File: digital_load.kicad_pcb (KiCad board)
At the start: 2 copper layers, 50 x 45 mm, 24 parts, among them J1 Conn_01x02, J2 Conn_01x02, J3 Conn_01x04, J4 Conn_01x04, J5 USB_C_Receptacle_USB2.0, Q20 BSB280N15NZ3, Q21 Q_NMOS_DGS, Q22 Q_NMOS_DGS, Q23 Q_NMOS_DGS, U10 PIC18F24K42, U20 LM358, U21 Adafruit_PiOLED

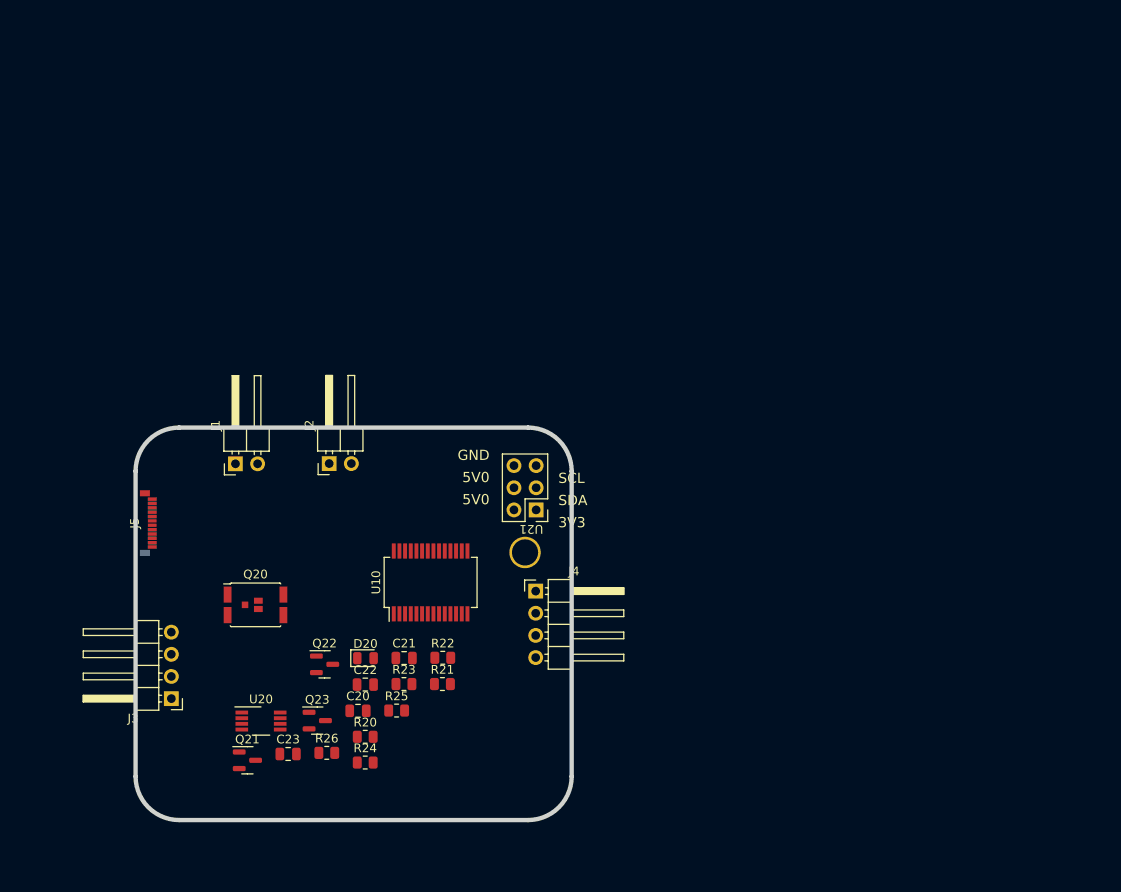
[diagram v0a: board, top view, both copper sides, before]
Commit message: Add uart usb controller
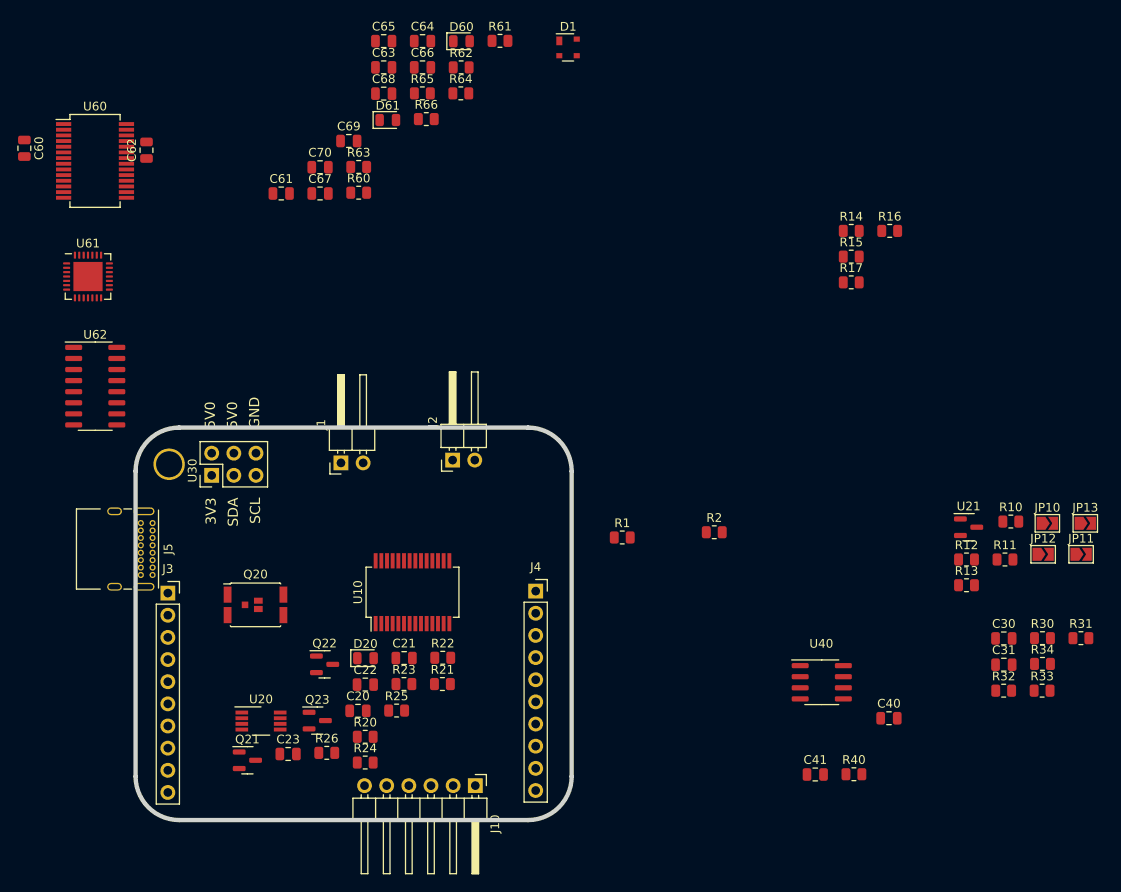
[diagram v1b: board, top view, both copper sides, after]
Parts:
- added C30: 10n, Capacitor_SMD:C_0805_2012Metric, F.Cu at (199.6, 109.2)
- added C31: 10n, Capacitor_SMD:C_0805_2012Metric, F.Cu at (199.6, 112.2)
- added C40: 1u, Capacitor_SMD:C_0805_2012Metric, F.Cu at (186.4, 118.3)
- added C41: 1u, Capacitor_SMD:C_0805_2012Metric, F.Cu at (177.9, 124.8)
- added C60: 4.7u, Capacitor_SMD:C_0805_2012Metric, F.Cu at (87.2, 53.0)
- added C61: 100n, Capacitor_SMD:C_0805_2012Metric, F.Cu at (116.7, 58.2)
- added C62: 100n, Capacitor_SMD:C_0805_2012Metric, F.Cu at (101.2, 53.2)
- added C63: 100n, Capacitor_SMD:C_0805_2012Metric, F.Cu at (128.4, 43.7)
- added C64: 100n, Capacitor_SMD:C_0805_2012Metric, F.Cu at (132.9, 40.7)
- added C65: 100n, Capacitor_SMD:C_0805_2012Metric, F.Cu at (128.4, 40.7)
- added C66: 4.7u, Capacitor_SMD:C_0805_2012Metric, F.Cu at (132.9, 43.7)
- added C67: 4.7u, Capacitor_SMD:C_0805_2012Metric, F.Cu at (121.2, 58.2)
- added C68: 10u, Capacitor_SMD:C_0805_2012Metric, F.Cu at (128.4, 46.7)
- added C69: 100n, Capacitor_SMD:C_0805_2012Metric, F.Cu at (124.5, 52.1)
- added C70: 100n, Capacitor_SMD:C_0805_2012Metric, F.Cu at (121.2, 55.1)
- added D1: SP0503BAHT, Package_TO_SOT_SMD:SOT-143, F.Cu at (149.6, 41.4)
- added D60: LED, LED_SMD:LED_0805_2012Metric, F.Cu at (137.4, 40.7)
- added D61: LED, LED_SMD:LED_0805_2012Metric, F.Cu at (128.9, 49.7)
- added J10: Conn_PIC_ICSP_ICD, Connector_PinHeader_2.54mm:PinHeader_1x06_P2.54mm_Horizontal, F.Cu at (138.9, 126.0)
- added JP10: SolderJumper_2_Open, Jumper:SolderJumper-2_P1.3mm_Open_TrianglePad1.0x1.5mm, F.Cu at (204.5, 96.0)
- added JP11: SolderJumper_2_Open, Jumper:SolderJumper-2_P1.3mm_Open_TrianglePad1.0x1.5mm, F.Cu at (208.4, 99.5)
- added JP12: SolderJumper_2_Open, Jumper:SolderJumper-2_P1.3mm_Open_TrianglePad1.0x1.5mm, F.Cu at (204.1, 99.5)
- added JP13: SolderJumper_2_Open, Jumper:SolderJumper-2_P1.3mm_Open_TrianglePad1.0x1.5mm, F.Cu at (208.9, 96.0)
- added R1: 5.1k, Resistor_SMD:R_0805_2012Metric, F.Cu at (155.8, 97.6)
- added R10: 10k, Resistor_SMD:R_0805_2012Metric, F.Cu at (200.3, 95.8)
- added R11: 10k, Resistor_SMD:R_0805_2012Metric, F.Cu at (199.7, 100.1)
- added R12: 10k, Resistor_SMD:R_0805_2012Metric, F.Cu at (195.3, 100.1)
- added R13: 10k, Resistor_SMD:R_0805_2012Metric, F.Cu at (195.3, 103.1)
- added R14: 10k, Resistor_SMD:R_0805_2012Metric, F.Cu at (182.1, 62.5)
- added R15: 10k, Resistor_SMD:R_0805_2012Metric, F.Cu at (182.1, 65.4)
- added R16: 10k, Resistor_SMD:R_0805_2012Metric, F.Cu at (186.5, 62.5)
- added R17: 4.7k, Resistor_SMD:R_0805_2012Metric, F.Cu at (182.1, 68.3)
- added R2: 5.1k, Resistor_SMD:R_0805_2012Metric, F.Cu at (166.3, 97.0)
- added R30: 10k, Resistor_SMD:R_0805_2012Metric, F.Cu at (204.0, 109.1)
- added R31: 10k, Resistor_SMD:R_0805_2012Metric, F.Cu at (208.4, 109.1)
- added R32: 10k, Resistor_SMD:R_0805_2012Metric, F.Cu at (199.5, 115.2)
- added R33: 10k, Resistor_SMD:R_0805_2012Metric, F.Cu at (203.9, 115.2)
- added R34: 10k, Resistor_SMD:R_0805_2012Metric, F.Cu at (204.0, 112.1)
- added R40: 10k, Resistor_SMD:R_0805_2012Metric, F.Cu at (182.4, 124.7)
- added R60: 4.7k, Resistor_SMD:R_0805_2012Metric, F.Cu at (125.6, 58.1)
- added R61: 10k, Resistor_SMD:R_0805_2012Metric, F.Cu at (141.8, 40.7)
- added R62: 22.1k, Resistor_SMD:R_0805_2012Metric, F.Cu at (137.3, 43.7)
- added R63: 47.5k, Resistor_SMD:R_0805_2012Metric, F.Cu at (125.6, 55.1)
- added R64: 1k, Resistor_SMD:R_0805_2012Metric, F.Cu at (137.3, 46.7)
- added R65: 10k, Resistor_SMD:R_0805_2012Metric, F.Cu at (132.9, 46.7)
- added R66: 10k, Resistor_SMD:R_0805_2012Metric, F.Cu at (133.3, 49.6)
- added U21: LM4040DBZ-2.0, Package_TO_SOT_SMD:SOT-23, F.Cu at (195.5, 96.4)
- added U40: LP2951-3.3_SOIC, Package_SO:SOIC-8_3.9x4.9mm_P1.27mm, F.Cu at (178.7, 114.2)
- added U60: FT232RL, Package_SO:SSOP-28_5.3x10.2mm_P0.65mm, F.Cu at (95.3, 54.4)
- added U61: CP2102N-Axx-xQFN28, Package_DFN_QFN:QFN-28-1EP_5x5mm_P0.5mm_EP3.35x3.35mm, F.Cu at (94.5, 67.7)
- added U62: CH340C, Package_SO:SOIC-16_3.9x9.9mm_P1.27mm, F.Cu at (95.4, 80.2)
- J3, J4: footprint Connector_PinHeader_2.54mm:PinHeader_1x04_P2.54mm_Horizontal -> Connector_PinSocket_2.54mm:PinSocket_1x10_P2.54mm_Vertical
- J5: footprint Connector_USB:USB_C_Plug_Molex_105444 -> Connector_USB:USB_C_Receptacle_GCT_USB4085
- moved U30 37.4 mm to (108.7, 90.5), turned to 90 degrees
- moved J2 14.2 mm to (136.3, 88.7)
- moved J3 12.1 mm to (103.7, 104.0), turned to 0 degrees
- moved J1 12.1 mm to (123.5, 89.0)
- moved U10 2.36 mm to (131.8, 103.9)
- renumbered U21 to U30
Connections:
- J3 pad 1: /Connectors/load_in -> /Connectors/I2C.SCL
- J3 pad 2: /Connectors/TXL -> /Connectors/I2C.SDA
- J3 pad 3: /Connectors/RXL -> +5V
- J3 pad 4: /Connectors/leader_present -> +5V
- J4 pad 2: /Connectors/TXR -> /Connectors/load_in
- J4 pad 3: /Connectors/RXR -> /Connectors/load_in
- J4 pad 4: /Connectors/follower_present -> /Connectors/load_in
- J5 pad A1: Net-(J5-PadA1) -> GND
- J5 pad A12: Net-(J5-PadA1) -> GND
- J5 pad A4: Net-(J5-PadA4) -> +5V
- J5 pad A5: unconnected-(J5-PadA5) -> Net-(J5-PadA5)
- J5 pad A6: unconnected-(J5-PadA6) -> /Connectors/USB2.0.D+
- J5 pad A7: unconnected-(J5-PadA7) -> /Connectors/USB2.0.D-
- J5 pad A9: Net-(J5-PadA4) -> +5V
- J5 pad B1: Net-(J5-PadA1) -> GND
- J5 pad B12: Net-(J5-PadA1) -> GND
- J5 pad B4: Net-(J5-PadA4) -> +5V
- J5 pad B5: unconnected-(J5-PadB5) -> Net-(J5-PadB5)
- J5 pad B9: Net-(J5-PadA4) -> +5V
- J5 pad S1: unconnected-(J5-PadS1) -> GND
- Q21 pad 2: /load_control/range_1ma -> /load_control/range.1ma
- Q22 pad 2: /load_control/range_100ma -> /load_control/range.100ma
- Q23 pad 2: /load_control/range_10a -> /load_control/range.10a
- U10 pad 1: unconnected-(U10-Pad1) -> /microcontroller/~{MCLR}/VPP
- U10 pad 10: unconnected-(U10-Pad10) -> /Display_Encoder/select
- U10 pad 14: /microcontroller/I2C.SCL -> /Connectors/I2C.SCL
- U10 pad 15: /microcontroller/I2C.SDA -> /Connectors/I2C.SDA
- U10 pad 17: /microcontroller/UARTL.TX -> unconnected-(U10-Pad17)
- U10 pad 18: /microcontroller/UARTL.RX -> unconnected-(U10-Pad18)
- U10 pad 21: /microcontroller/pwm_ctrl -> /load_control/pwm_ctrl
- U10 pad 22: /microcontroller/range_1ma -> /load_control/range.1ma
- U10 pad 23: /microcontroller/range_100ma -> /load_control/range.100ma
- U10 pad 24: /microcontroller/range_10a -> /load_control/range.10a
- U10 pad 25: unconnected-(U10-Pad25) -> /load_control/current_measure
- U10 pad 27: /microcontroller/UARTR.TX -> /microcontroller/ICSPCLK
- U10 pad 28: /microcontroller/UARTR.RX -> /microcontroller/ICSPDAT
- U10 pad 5: unconnected-(U10-Pad5) -> /microcontroller/2.048V
- U10 pad 6: unconnected-(U10-Pad6) -> /microcontroller/3V3_sense
- U10 pad 7: unconnected-(U10-Pad7) -> /microcontroller/5V_sense
- U30 pad 3: /Display/I2C.SDA -> /Connectors/I2C.SDA
- U30 pad 5: /Display/I2C.SCL -> /Connectors/I2C.SCL

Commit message: Fix lots of small things
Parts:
- added C10: 100n, Capacitor_SMD:C_0805_2012Metric, F.Cu at (108.7, 50.2)
- added SW30: PEC11R, Rotary_Encoder:RotaryEncoder_Alps_EC12E-Switch_Vertical_H20mm, F.Cu at (164.8, 81.5)
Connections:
- C60 pad 1: /Connectors/USB2.0.VBUS -> +5V
- C62 pad 1: /Connectors/USB2.0.VBUS -> +5V
- C63 pad 1: /Connectors/USB2.0.VBUS -> +5V
- C64 pad 1: /Connectors/USB2.0.VBUS -> +5V
- C65 pad 1: /Connectors/USB2.0.VBUS -> +5V
- C66 pad 1: /Connectors/USB2.0.VBUS -> +5V
- C67 pad 1: /Connectors/USB2.0.VBUS -> +5V
- C68 pad 1: /Connectors/USB2.0.VBUS -> +5V
- C69 pad 1: /Connectors/USB2.0.VBUS -> +5V
- D60 pad 2: /Connectors/USB2.0.VBUS -> +5V
- D61 pad 2: /Connectors/USB2.0.VBUS -> +5V
- Q20 pad 1: /load_control/load_in -> /Connectors/load_in
- R60 pad 2: /Connectors/USB2.0.VBUS -> +5V
- R62 pad 2: /Connectors/USB2.0.VBUS -> +5V
- R64 pad 2: /Connectors/USB2.0.VBUS -> +5V
- U10 pad 10: /Display_Encoder/select -> unconnected-(U10-Pad10)
- U10 pad 13: unconnected-(U10-Pad13) -> /microcontroller/UART.RTS
- U10 pad 16: unconnected-(U10-Pad16) -> /microcontroller/UART.TX
- U10 pad 17: unconnected-(U10-Pad17) -> /microcontroller/UART.CTS
- U10 pad 18: unconnected-(U10-Pad18) -> /microcontroller/UART.RX
- U10 pad 21: /load_control/pwm_ctrl -> /Display_Encoder/ENC.B
- U10 pad 26: unconnected-(U10-Pad26) -> /load_control/pwm_ctrl
- U10 pad 3: unconnected-(U10-Pad3) -> /Display_Encoder/select
- U10 pad 4: unconnected-(U10-Pad4) -> /Display_Encoder/ENC.A
- U60 pad 20: /Connectors/USB2.0.VBUS -> +5V
- U60 pad 4: /Connectors/USB2.0.VBUS -> +5V
- U61 pad 6: /Connectors/USB2.0.VBUS -> +5V
- U61 pad 7: /Connectors/USB2.0.VBUS -> +5V
- U62 pad 16: /Connectors/USB2.0.VBUS -> +5V

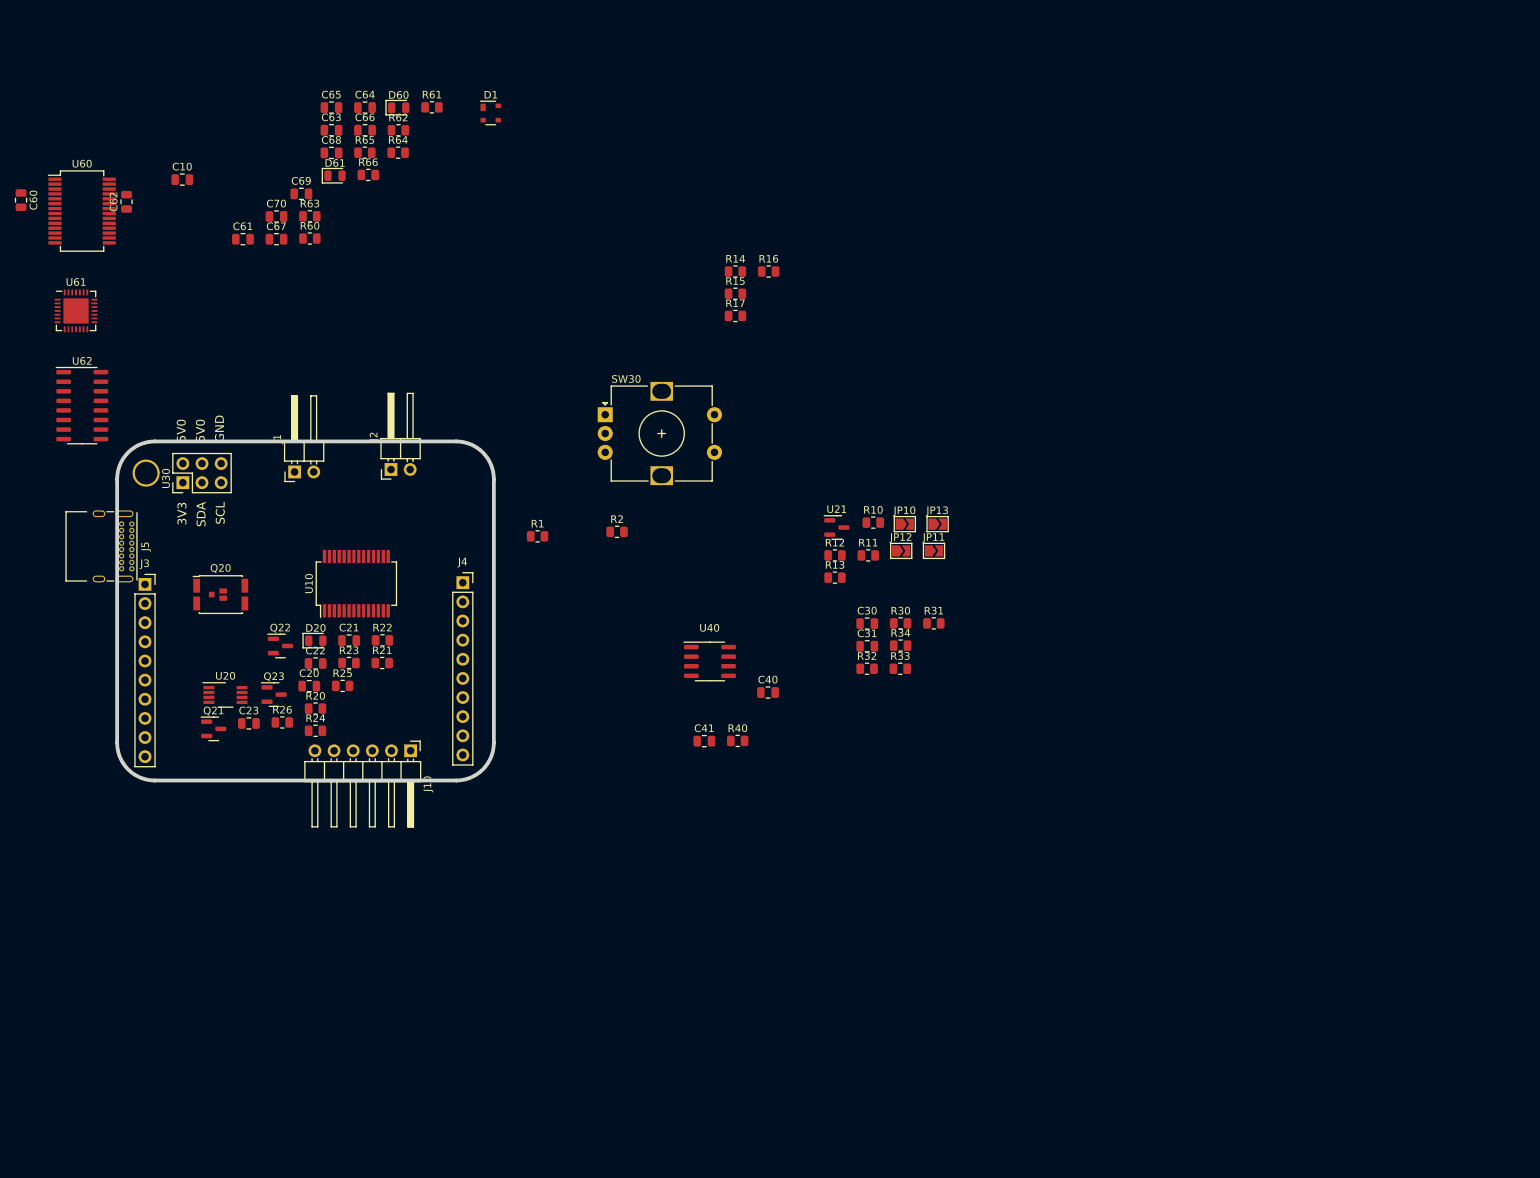
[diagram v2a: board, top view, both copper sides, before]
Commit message: Arrange components of subcircuits
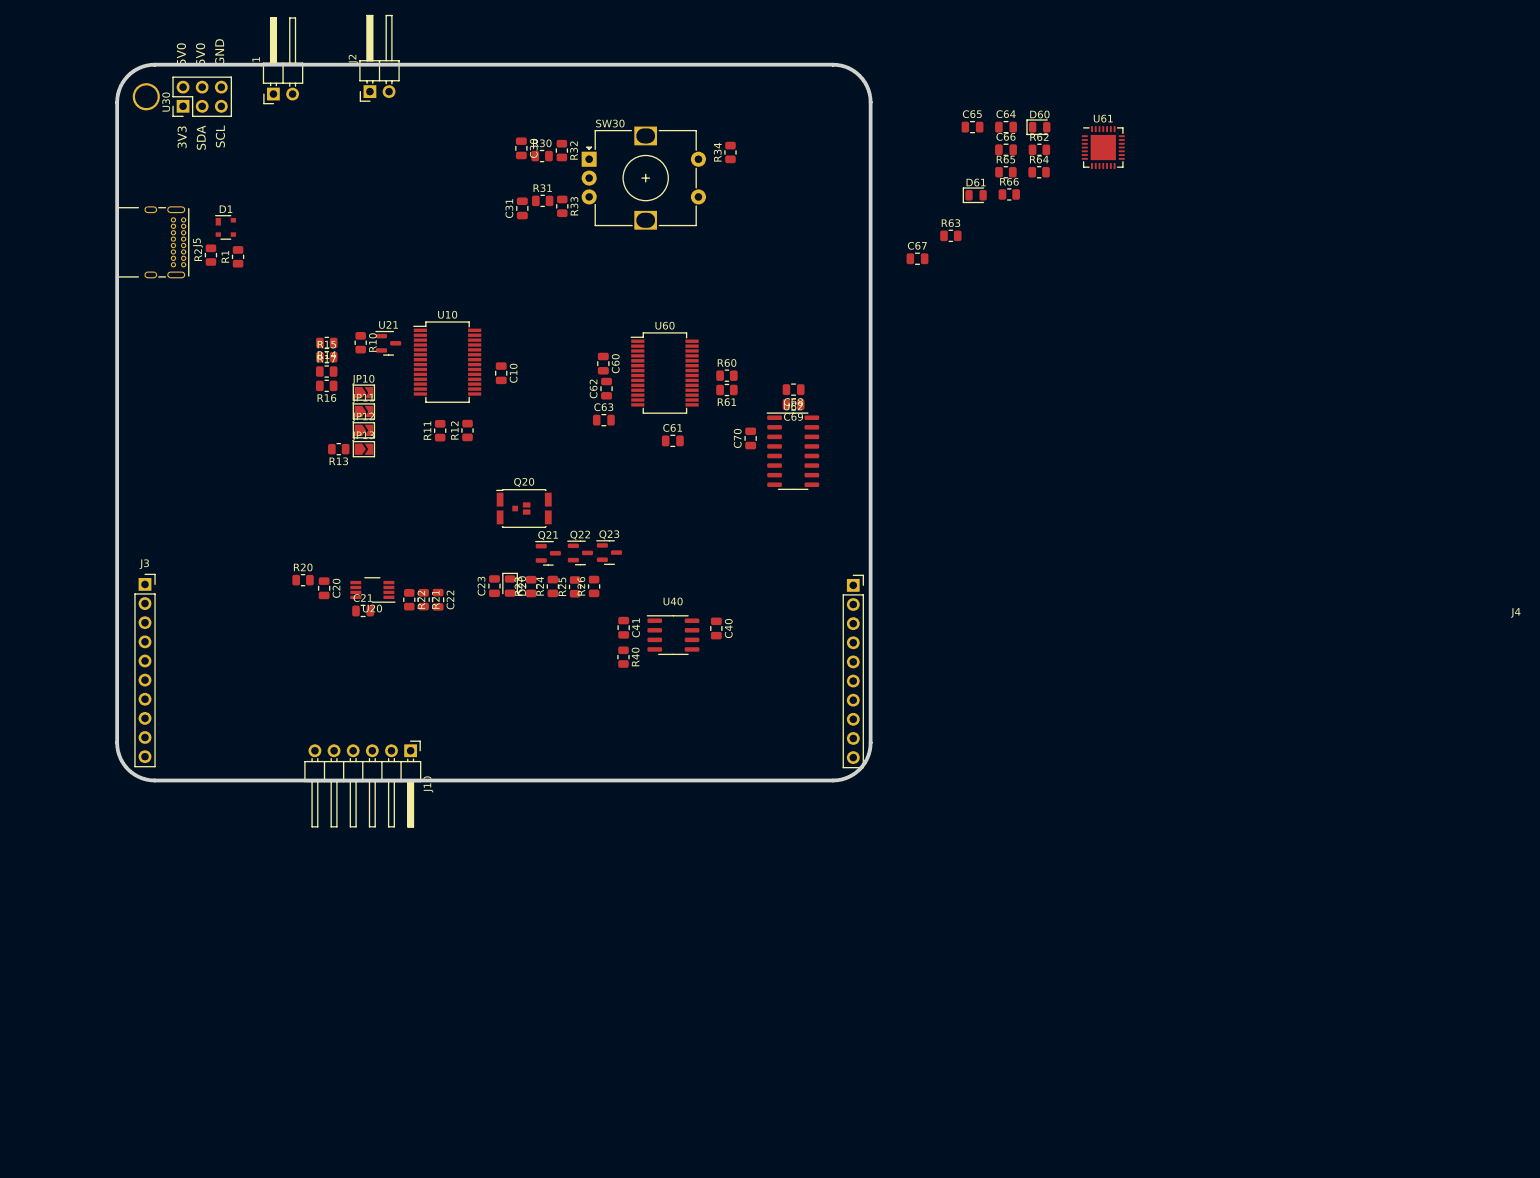
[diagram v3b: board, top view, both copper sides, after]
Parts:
- R11, R12: value 10k -> 4.7k
- moved U61 138.0 mm to (230.9, 46.0)
- moved U62 94.5 mm to (189.7, 86.3)
- moved C65 85.1 mm to (213.5, 43.3)
- moved D61 85.1 mm to (214.0, 52.3)
- moved R64 85.1 mm to (222.4, 49.3)
- moved R63 85.1 mm to (210.7, 57.7)
- moved C64 85.1 mm to (218.0, 43.3)
- moved C66 85.1 mm to (218.0, 46.3)
- moved C67 85.1 mm to (206.2, 60.8)
- moved D60 85.1 mm to (222.4, 43.3)
- moved R62 85.1 mm to (222.4, 46.3)
- moved R65 85.1 mm to (217.9, 49.3)
- moved R66 85.1 mm to (218.4, 52.2)
- moved U60 80.3 mm to (172.7, 75.9)
- moved C60 80.3 mm to (164.5, 74.7)
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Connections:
- R33 pad 1: Net-(R30-Pad2) -> Net-(R31-Pad2)
- U10 pad 10: unconnected-(U10-Pad10) -> /microcontroller/I2C_A1
- U10 pad 11: unconnected-(U10-Pad11) -> /microcontroller/I2C_A2
- U10 pad 12: unconnected-(U10-Pad12) -> /microcontroller/I2C_A3
- U10 pad 9: unconnected-(U10-Pad9) -> /microcontroller/I2C_A0
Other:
- board size 50 x 45 mm -> 100 x 95 mm
